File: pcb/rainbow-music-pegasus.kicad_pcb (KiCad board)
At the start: 2 copper layers, 32 parts, among them J1 USB_B_Micro, J2 Conn_02x03_Odd_Even, U1 ESP32-C3-MINI-1, U2 OPA340NA, U3 AP2204RB-3.3

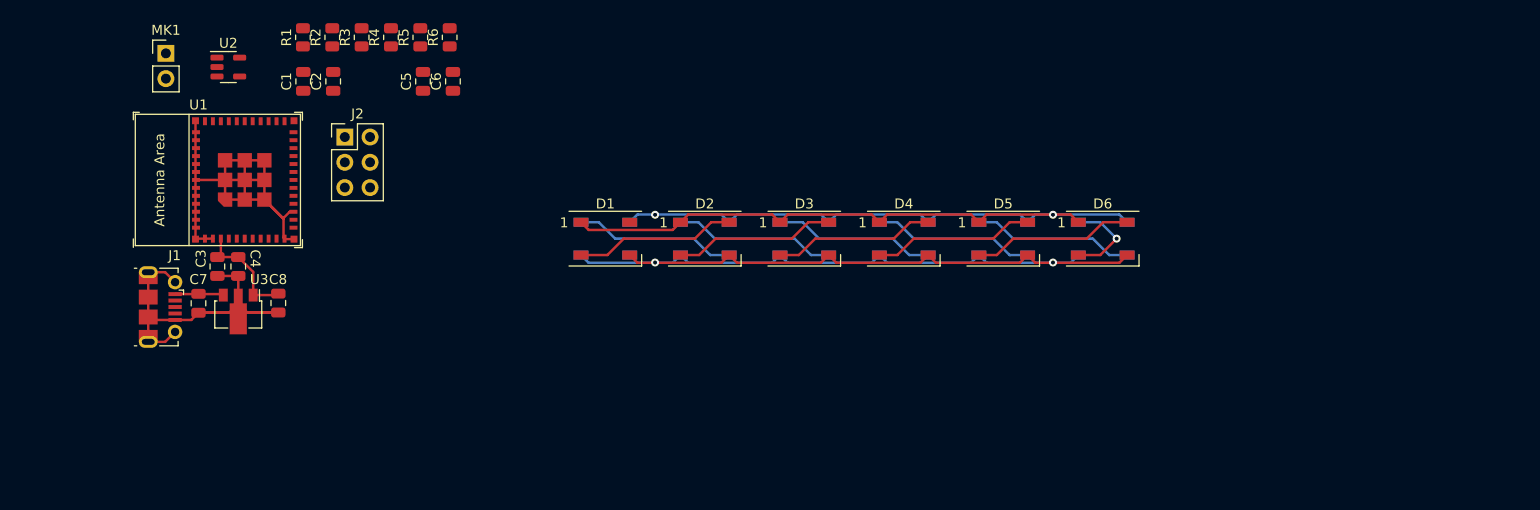
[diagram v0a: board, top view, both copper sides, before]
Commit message: Working PCB design using esp32c3 and 20 ws2812b LEDs -- BOM pending validation
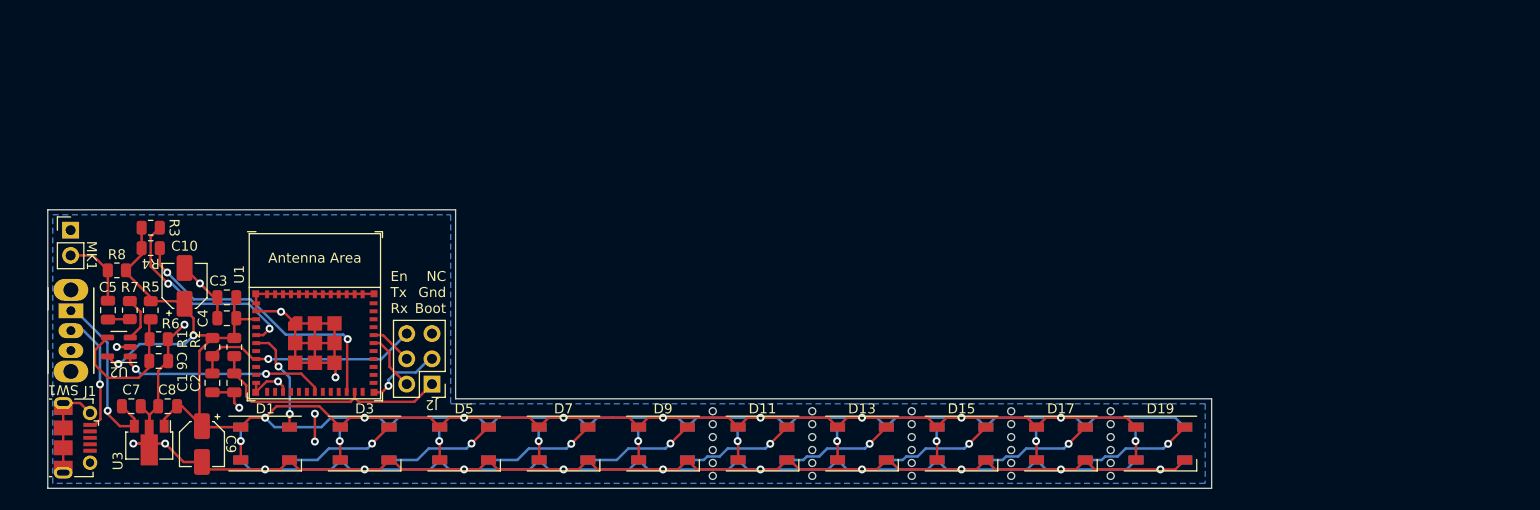
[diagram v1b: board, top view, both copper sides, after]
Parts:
- added C10: 220uF, Capacitor_SMD:CP_Elec_4x3, F.Cu at (97.7, 84.8)
- added C9: 220uF, Capacitor_SMD:CP_Elec_4x3, F.Cu at (99.5, 100.7)
- added D13: WS2812B, LED_SMD:LED_WS2812B_PLCC4_5.0x5.0mm_P3.2mm, F.Cu at (165.8, 100.6)
- added D14: WS2812B, LED_SMD:LED_WS2812B_PLCC4_5.0x5.0mm_P3.2mm, B.Cu at (165.8, 100.6)
- added D15: WS2812B, LED_SMD:LED_WS2812B_PLCC4_5.0x5.0mm_P3.2mm, F.Cu at (175.8, 100.6)
- added D16: WS2812B, LED_SMD:LED_WS2812B_PLCC4_5.0x5.0mm_P3.2mm, B.Cu at (175.8, 100.6)
- added D17: WS2812B, LED_SMD:LED_WS2812B_PLCC4_5.0x5.0mm_P3.2mm, F.Cu at (185.8, 100.6)
- added D18: WS2812B, LED_SMD:LED_WS2812B_PLCC4_5.0x5.0mm_P3.2mm, B.Cu at (185.8, 100.6)
- added D19: WS2812B, LED_SMD:LED_WS2812B_PLCC4_5.0x5.0mm_P3.2mm, F.Cu at (195.8, 100.6)
- added D20: WS2812B, LED_SMD:LED_WS2812B_PLCC4_5.0x5.0mm_P3.2mm, B.Cu at (195.8, 100.6)
- added R3: 10k, Resistor_SMD:R_0805_2012Metric, F.Cu at (94.3, 78.9)
- added R4: 10k, Resistor_SMD:R_0805_2012Metric, F.Cu at (94.3, 81.0)
- added SW1: SW_SPDT, Button_Switch_THT:SW_CuK_OS102011MA1QN1_SPDT_Angled, F.Cu at (86.3, 87.2)
- D11, D7, D9: moved to F.Cu
- D2, D4, D6: moved to B.Cu
- moved D6 67.4 mm to (125.8, 100.6), turned to 180 degrees
- moved D4 58.0 mm to (115.8, 100.6), turned to 180 degrees
- moved D5 58.0 mm to (125.8, 100.6)
- moved D7 58.0 mm to (135.8, 100.6), turned to 0 degrees
- moved D2 48.8 mm to (105.8, 100.6), turned to 180 degrees
- moved D3 48.8 mm to (115.8, 100.6)
- moved D8 48.8 mm to (135.8, 100.6)
- moved R6 42.1 mm to (95.1, 90.1), turned to 180 degrees
- moved C6 40.8 mm to (95.1, 92.3), turned to 180 degrees
- moved D1 39.9 mm to (105.8, 100.6)
- moved C5 39.1 mm to (90.0, 87.2), turned to -90 degrees
- moved R5 38.6 mm to (94.3, 87.2)
- moved R7 38.0 mm to (92.2, 87.2)
- moved R8 34.0 mm to (90.9, 83.2), turned to 180 degrees
- moved R2 32.7 mm to (102.7, 90.9), turned to -90 degrees
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- renumbered R4 to R7, R3 to R8
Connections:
- C7 pad 2: Net-(J1-VBUS) -> Net-(SW1-A)
- D12 pad 2: unconnected-(D12-DOUT-Pad2) -> Net-(D12-DOUT)
- U1 pad 18: unconnected-(U1-GPIO4/ADC1_CH4-Pad18) -> /Mic_Signal
- U1 pad 20: /RGB_Data -> unconnected-(U1-GPIO6-Pad20)
- U1 pad 22: unconnected-(U1-GPIO8-Pad22) -> Net-(U1-GPIO8)
- U1 pad 5: unconnected-(U1-GPIO2/ADC1_CH2-Pad5) -> Net-(U1-GPIO2/ADC1_CH2)
- U1 pad 6: /Mic_Signal -> /RGB_Data
- U3 pad 3: Net-(J1-VBUS) -> Net-(SW1-A)
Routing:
- net +3.3V: track 117.6 -> 253.2 mm, vias 2 -> 11
- net GND: track 195.8 -> 308.6 mm, vias 2 -> 22
- net Net-(U1-GPIO8): track 0.00 -> 29.0 mm, vias 0 -> 2
- net /Boot: track 0.00 -> 25.1 mm
- net /Reset: track 0.00 -> 23.2 mm, vias 0 -> 1
- net /Mic_Signal: track 0.00 -> 20.7 mm, vias 0 -> 2
- net Net-(U1-GPIO2/ADC1_CH2): track 0.00 -> 20.6 mm, vias 0 -> 2
- net Net-(SW1-A): track 0.00 -> 19.2 mm, vias 0 -> 1
- net Net-(U2--): track 0.00 -> 14.6 mm
- net Net-(D1-DOUT): track 16.3 -> 3.30 mm, vias 0 -> 1
- net Net-(D7-DOUT): track 16.3 -> 3.34 mm, vias 0 -> 1
- net Net-(D11-DOUT): track 16.3 -> 3.34 mm, vias 0 -> 1
- net Net-(D10-DIN): track 16.3 -> 3.34 mm, vias 0 -> 1
- net Net-(D5-DOUT): track 16.3 -> 3.34 mm, vias 0 -> 1
- net Net-(D3-DOUT): track 16.3 -> 3.34 mm, vias 0 -> 1
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- added copper zone on B.Cu, net GND
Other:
- board outline added: 117 x 28 mm
- board text added: "En Tx Rx"
- board text added: "NC Gnd Boot"
- board text added: "Rainbow Music Pegasus"

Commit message: Finalize PCB layout for first production run
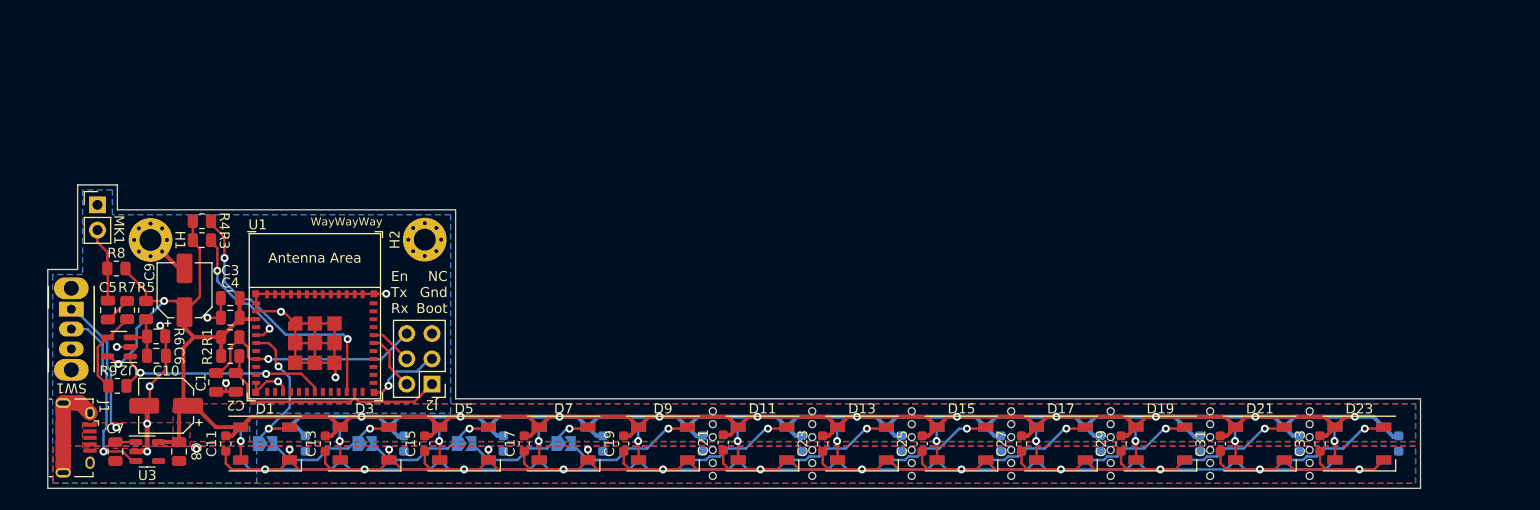
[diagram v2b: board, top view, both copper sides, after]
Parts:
- added C11: 0.1uF, Capacitor_SMD:C_0603_1608Metric, F.Cu at (101.8, 100.6)
- added C12: 0.1uF, Capacitor_SMD:C_0603_1608Metric, B.Cu at (109.8, 100.6)
- added C13: 0.1uF, Capacitor_SMD:C_0603_1608Metric, F.Cu at (111.8, 100.6)
- added C14: 0.1uF, Capacitor_SMD:C_0603_1608Metric, B.Cu at (119.7, 100.6)
- added C15: 0.1uF, Capacitor_SMD:C_0603_1608Metric, F.Cu at (121.8, 100.6)
- added C16: 0.1uF, Capacitor_SMD:C_0603_1608Metric, B.Cu at (129.7, 100.6)
- added C17: 0.1uF, Capacitor_SMD:C_0603_1608Metric, F.Cu at (131.8, 100.6)
- added C18: 0.1uF, Capacitor_SMD:C_0603_1608Metric, B.Cu at (139.7, 100.6)
- added C19: 0.1uF, Capacitor_SMD:C_0603_1608Metric, F.Cu at (141.8, 100.6)
- added C20: 0.1uF, Capacitor_SMD:C_0603_1608Metric, B.Cu at (149.7, 100.6)
- added C21: 0.1uF, Capacitor_SMD:C_0603_1608Metric, F.Cu at (151.8, 100.5)
- added C22: 0.1uF, Capacitor_SMD:C_0603_1608Metric, B.Cu at (159.7, 100.6)
- added C23: 0.1uF, Capacitor_SMD:C_0603_1608Metric, F.Cu at (161.8, 100.6)
- added C24: 0.1uF, Capacitor_SMD:C_0603_1608Metric, B.Cu at (179.7, 100.6)
- added C25: 0.1uF, Capacitor_SMD:C_0603_1608Metric, F.Cu at (171.8, 100.6)
- added C26: 0.1uF, Capacitor_SMD:C_0603_1608Metric, B.Cu at (169.7, 100.6)
- added C27: 0.1uF, Capacitor_SMD:C_0603_1608Metric, F.Cu at (181.8, 100.6)
- added C28: 0.1uF, Capacitor_SMD:C_0603_1608Metric, B.Cu at (189.7, 100.6)
- added C29: 0.1uF, Capacitor_SMD:C_0603_1608Metric, F.Cu at (191.8, 100.6)
- added C30: 0.1uF, Capacitor_SMD:C_0603_1608Metric, B.Cu at (199.8, 100.6)
- added C31: 0.1uF, Capacitor_SMD:C_0603_1608Metric, F.Cu at (201.8, 100.6)
- added C32: 0.1uF, Capacitor_SMD:C_0603_1608Metric, B.Cu at (209.8, 100.6)
- added C33: 0.1uF, Capacitor_SMD:C_0603_1608Metric, F.Cu at (211.8, 100.6)
- added C34: 0.1uF, Capacitor_SMD:C_0603_1608Metric, B.Cu at (219.8, 100.6)
- added D21: WS2812B, LED_SMD:LED_WS2812B_PLCC4_5.0x5.0mm_P3.2mm, F.Cu at (205.8, 100.6)
- added D22: WS2812B, LED_SMD:LED_WS2812B_PLCC4_5.0x5.0mm_P3.2mm, B.Cu at (205.8, 100.6)
- added D23: WS2812B, LED_SMD:LED_WS2812B_PLCC4_5.0x5.0mm_P3.2mm, F.Cu at (215.8, 100.6)
- added D24: WS2812B, LED_SMD:LED_WS2812B_PLCC4_5.0x5.0mm_P3.2mm, B.Cu at (215.8, 100.6)
- added H1: MountingHole_Pad, MountingHole:MountingHole_2.2mm_M2_Pad_Via, F.Cu at (94.3, 80.1)
- added H2: MountingHole_Pad, MountingHole:MountingHole_2.2mm_M2_Pad_Via, F.Cu at (121.8, 80.1)
- added JP1: SolderJumper, Jumper:SolderJumper-2_P1.3mm_Open_TrianglePad1.0x1.5mm, B.Cu at (105.8, 100.6)
- added JP2: SolderJumper, Jumper:SolderJumper-2_P1.3mm_Open_TrianglePad1.0x1.5mm, B.Cu at (115.8, 100.6)
- added JP3: SolderJumper, Jumper:SolderJumper-2_P1.3mm_Open_TrianglePad1.0x1.5mm, B.Cu at (125.8, 100.6)
- added JP4: SolderJumper, Jumper:SolderJumper-2_P1.3mm_Open_TrianglePad1.0x1.5mm, B.Cu at (135.8, 100.6)
- added R9: 820k, Resistor_SMD:R_0805_2012Metric, F.Cu at (90.9, 94.8)
- added REF**: OSHW-Logo2_9.8x8mm_SilkScreen, Symbol:OSHW-Logo2_9.8x8mm_SilkScreen, B.Cu at (97.1, 89.5)
- C10: renamed from C9; footprint Capacitor_SMD:CP_Elec_4x3 -> Capacitor_SMD:CP_Elec_5x5.9
- C9: renamed from C10; footprint Capacitor_SMD:CP_Elec_4x3 -> Capacitor_SMD:CP_Elec_5x5.9
- R1, R2: value 10K -> 10k
- U2: value OPA340NA -> OPA344NA
- U3: value AP2204RB-3.3 -> TLV75533PDBV; footprint Package_TO_SOT_SMD:SOT-89-3 -> Package_TO_SOT_SMD:SOT-23-5
- moved R4 5.81 mm to (99.4, 78.2)
- moved R3 5.30 mm to (99.4, 80.2)
- moved C10 5.27 mm to (95.8, 96.8), turned to 180 degrees
- moved C7 4.82 mm to (90.7, 101.4), turned to 90 degrees
- moved C8 4.69 mm to (97.1, 101.4), turned to 90 degrees
- moved MK1 3.71 mm to (88.9, 76.6)
- moved R1 2.06 mm to (102.3, 89.9), turned to 0 degrees
- moved R2 0.99 mm to (102.3, 91.8), turned to 0 degrees
- moved U3 0.63 mm to (93.9, 101.4), turned to 0 degrees
- moved C6 0.57 mm to (94.9, 91.8)
- moved R5 0.47 mm to (93.8, 87.2)
- moved C9 0.44 mm to (97.7, 85.2)
- moved C1 0.38 mm to (100.9, 94.5)
- moved R6 0.37 mm to (94.8, 89.8)
- moved C3 0.36 mm to (102.3, 86.0)
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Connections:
- C6 pad 2: Net-(U2--) -> Net-(U2-+)
- C7 pad 2: Net-(SW1-A) -> Net-(J1-VBUS)
- D20 pad 2: unconnected-(D20-DOUT-Pad2) -> Net-(D20-DOUT)
- R5 pad 1: Net-(U2--) -> Net-(U2-+)
- R6 pad 2: Net-(U2--) -> Net-(U2-+)
- R7 pad 2: Net-(U2-+) -> Net-(U2--)
- SW1 pad 1: Net-(SW1-A) -> Net-(J1-VBUS)
- SW1 pad 2: Net-(J1-VBUS) -> Net-(SW1-B)
- SW1 pad 3: unconnected-(SW1-C-Pad3) -> GND
- U3 pad 1: +3.3V -> Net-(J1-VBUS)
- U3 pad 3: Net-(SW1-A) -> Net-(SW1-B)
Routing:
- net +3.3V: track 253.2 -> 351.2 mm, vias 11 -> 13
- net GND: track 308.6 -> 395.1 mm, vias 22 -> 29
- net Net-(SW1-A): track 19.2 -> 0.00 mm, vias 1 -> 0
- net Net-(SW1-B): track 0.00 -> 18.5 mm, vias 0 -> 1
- net Net-(D22-DOUT): track 0.00 -> 11.4 mm, vias 0 -> 1
- net Net-(D20-DOUT): track 0.00 -> 11.4 mm, vias 0 -> 1
- net Net-(U1-GPIO2/ADC1_CH2): track 20.6 -> 13.5 mm
- net Net-(U2--): track 14.6 -> 8.44 mm
- net /RGB_Data: track 10.6 -> 15.7 mm
- net Net-(J1-VBUS): track 12.2 -> 16.0 mm
- net Net-(D23-DOUT): track 0.00 -> 3.34 mm, vias 0 -> 1
- net Net-(D21-DOUT): track 0.00 -> 3.34 mm, vias 0 -> 1
- net Net-(D6-DOUT): track 11.4 -> 13.8 mm
- net Net-(D4-DOUT): track 11.4 -> 13.8 mm
- net Net-(D8-DOUT): track 11.4 -> 13.8 mm
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- added copper zone on B.Cu, net +3.3V
- added copper zone on F.Cu, net +3.3V
- added copper zone on F.Cu, net GND
- added copper zone on F.Cu, net Net-(J1-VBUS)
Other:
- board size 117 x 28 mm -> 138 x 30.5 mm
- board text added: "Epic Fail Studios"
- board text added: "WayWayWay"
- board text added: "github.com/adamm/rainbow-music-pegasus"
- board text added: "v1"

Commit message: Added a few test points for power.  Committing gerbers
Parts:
- added TP1: TestPoint, TestPoint:TestPoint_THTPad_1.5x1.5mm_Drill0.7mm, F.Cu at (90.5, 98.4)
- added TP2: TestPoint, TestPoint:TestPoint_THTPad_1.5x1.5mm_Drill0.7mm, F.Cu at (110.8, 97.6)
- added TP3: TestPoint, TestPoint:TestPoint_THTPad_1.5x1.5mm_Drill0.7mm, F.Cu at (110.8, 103.6)
- moved R8 0.72 mm to (91.5, 83.2)
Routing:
- net Net-(J1-VBUS): track 16.0 -> 19.8 mm, vias 1 -> 0
- net +3.3V: track 351.2 -> 350.7 mm
- net Net-(MK1-+): track 7.52 -> 8.06 mm
- net GND: vias 29 -> 28

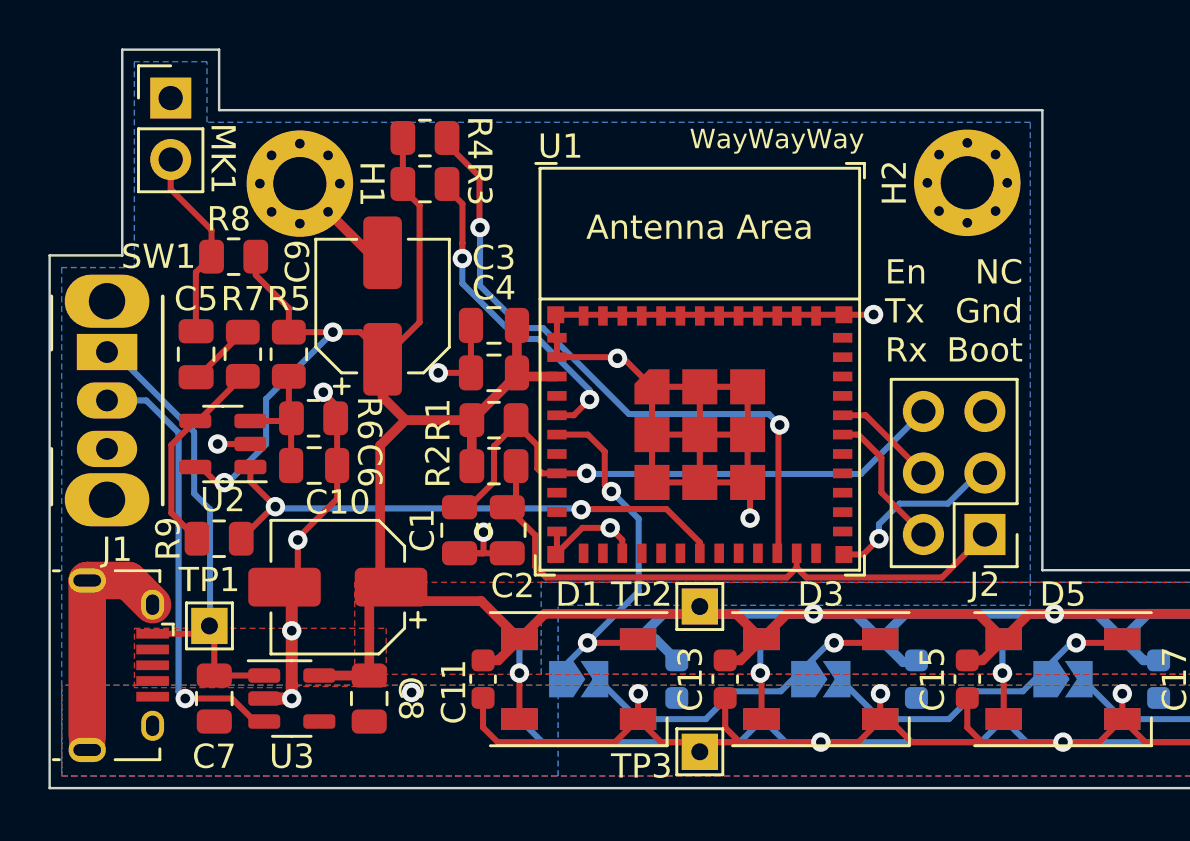
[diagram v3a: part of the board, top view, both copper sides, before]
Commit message: Added Altivo cartoon to silkscreen, jumpers for configuring total LEDs installed
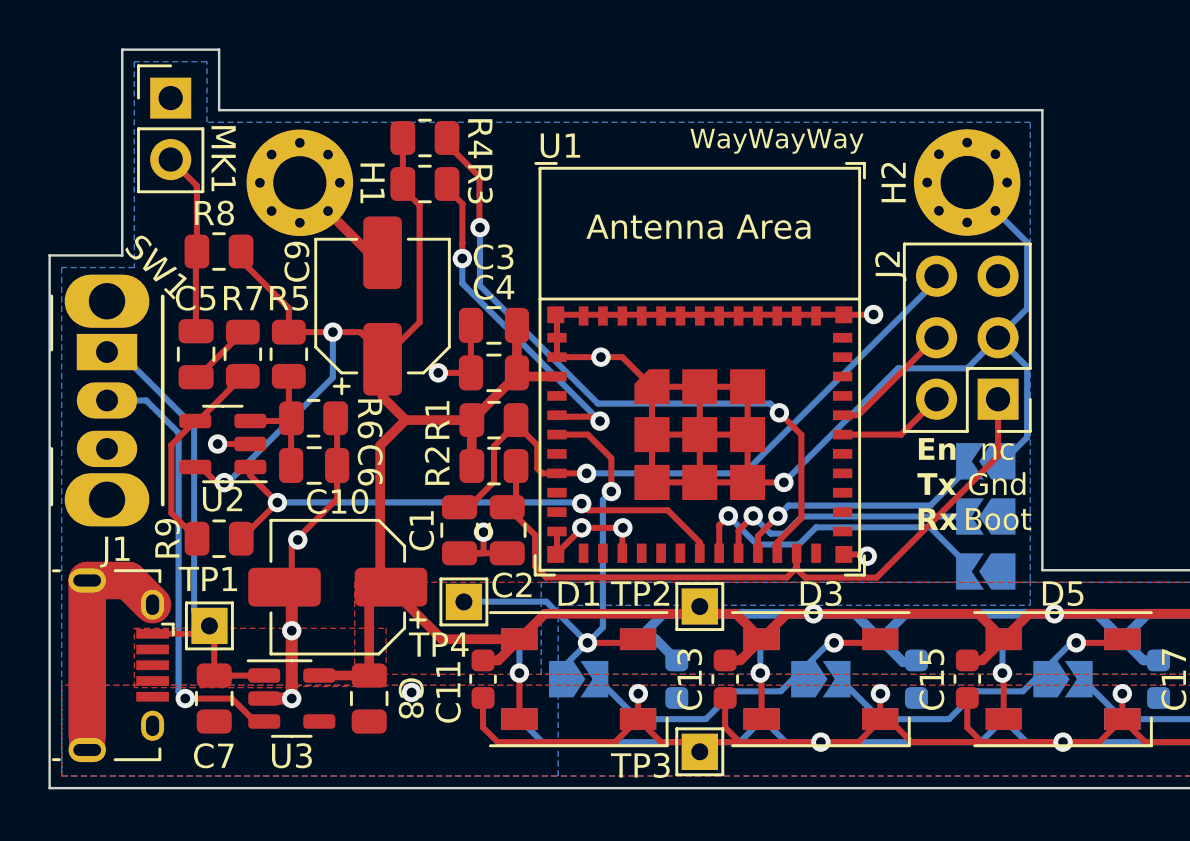
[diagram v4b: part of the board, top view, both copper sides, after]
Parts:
- removed REF**: OSHW-Logo2_9.8x8mm_SilkScreen, Symbol:OSHW-Logo2_9.8x8mm_SilkScreen
- added G***: Altivo, Altivo:altivo, B.Cu at (96.9, 95.0)
- added JP5: SolderJumper, Jumper:SolderJumper-2_P1.3mm_Open_TrianglePad1.0x1.5mm, B.Cu at (122.6, 91.6)
- added JP6: SolderJumper, Jumper:SolderJumper-2_P1.3mm_Open_TrianglePad1.0x1.5mm, B.Cu at (122.6, 93.9)
- added JP7: SolderJumper, Jumper:SolderJumper-2_P1.3mm_Open_TrianglePad1.0x1.5mm, B.Cu at (122.6, 96.2)
- added TP4: TestPoint, TestPoint:TestPoint_THTPad_1.5x1.5mm_Drill0.7mm, F.Cu at (101.1, 97.4)
- moved J2 5.61 mm to (123.1, 89.0)
- moved R8 0.64 mm to (90.9, 82.9)
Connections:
- U1 pad 19: unconnected-(U1-GPIO5/ADC2_CH0-Pad19) -> /LEDs+8
- U1 pad 20: unconnected-(U1-GPIO6-Pad20) -> /LEDs+4
- U1 pad 21: unconnected-(U1-GPIO7-Pad21) -> /LEDs+2
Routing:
- net GND: track 395.1 -> 413.6 mm
- net /LEDs+8: track 0.00 -> 13.3 mm, vias 0 -> 1
- net /LEDs+4: track 0.00 -> 11.3 mm, vias 0 -> 1
- net /LEDs+2: track 0.00 -> 10.8 mm, vias 0 -> 1
- net /RGB_Data: track 15.7 -> 20.6 mm
- net /Boot: track 25.2 -> 30.1 mm
- net /Reset: track 24.3 -> 27.2 mm
- net /RXD: track 5.89 -> 4.48 mm
- net Net-(U1-GPIO8): track 26.8 -> 27.8 mm
- net /TXD: track 4.32 -> 5.20 mm
- net Net-(U1-GPIO2/ADC1_CH2): track 13.5 -> 14.3 mm
- net Net-(MK1-+): track 8.06 -> 7.56 mm
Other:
- board text added: "+2"
- board text added: "+4"
- board text added: "+8"
- board text added: "10"
- board text added: "nc Gnd Boot"
- board text removed: "NC Gnd Boot"
